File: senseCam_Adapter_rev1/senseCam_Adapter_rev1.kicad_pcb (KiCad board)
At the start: 2 copper layers, 66 x 46 mm, 11 parts, among them J1 Conn_01x30, J2 Conn_01x30, J3 Conn_01x08, J4 Conn_01x06, P1 CONN_02X05, Q1 Q_PMOS_DGS, SW1 SW_SPST, SW2 SW_Push

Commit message: SenseCam adapter board done
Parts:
- added C10: 0.1nF, sense:C_0805, F.Cu at (28.5, 38.5)
- added C12: 100nF, sense:C_0805, F.Cu at (98.0, 20.5)
- added C13: 100nF, sense:C_0805, F.Cu at (43.5, 20.5)
- added C14: 100nF, sense:C_0805, F.Cu at (30.5, 20.5)
- added C15: 100nF, sense:C_0805, F.Cu at (85.5, 20.5)
- added C3: 0.47uF, sense:C_0805, F.Cu at (89.0, 21.0)
- added C4: 0.47uF, sense:C_0805, F.Cu at (34.5, 21.0)
- added C5: 0.1nF, sense:C_0805, F.Cu at (96.0, 38.5)
- added C6: 0.1nF, sense:C_0805, F.Cu at (41.5, 38.5)
- added C7: 0.47uF, sense:C_0805, F.Cu at (76.5, 21.0)
- added C8: 0.47uF, sense:C_0805, F.Cu at (21.5, 21.0)
- added C9: 0.1nF, sense:C_0805, F.Cu at (83.5, 38.5)
- added G***: LOGO, sense:OSHW1, B.Cu at (69.4, 35.7)
- added G***: Appiko_LOGO_img, sense:Appiko_LOGO_img, F.Cu at (61.9, 28.4)
- added J5: LDR_CONN, sense:Pin_Header_Straight_1x02_Pitch2.54mm, F.Cu at (21.0, 52.0)
- added J6: Conn_01x03, sense:TerminalBlock_bornier-3_P5.08mm, F.Cu at (84.0, 14.5)
- added J7: Conn_01x03, sense:TerminalBlock_bornier-3_P5.08mm, F.Cu at (28.0, 14.5)
- added J8: Conn_01x02, sense:PinHeader_1x02_P2.54mm_Vertical, F.Cu at (63.3, 51.9)
- added R1: 10k, sense:R_0805, F.Cu at (20.0, 49.5)
- added R2: 0R033, sense:R_2512_6332Metric_Pad1.52x3.35mm_HandSolder, F.Cu at (91.0, 38.5)
- added R3: 0R033, sense:R_2512_6332Metric_Pad1.52x3.35mm_HandSolder, F.Cu at (36.5, 38.5)
- added R4: 0R033, sense:R_2512_6332Metric_Pad1.52x3.35mm_HandSolder, F.Cu at (78.5, 38.5)
- added R5: 0R033, sense:R_2512_6332Metric_Pad1.52x3.35mm_HandSolder, F.Cu at (23.5, 38.5)
- added U1: STCS2A, sense:STCS2A_PowerSO-10, F.Cu at (94.0, 28.0)
- added U2: STCS2A, sense:STCS2A_PowerSO-10, F.Cu at (39.5, 28.0)
- added U3: STCS2A, sense:STCS2A_PowerSO-10, F.Cu at (81.5, 28.0)
- added U4: STCS2A, sense:STCS2A_PowerSO-10, F.Cu at (26.5, 28.0)
- BT1: value Battery -> LiPo 2s; footprint sense:Molex_KK-6410-02_02x2.54mm_Straight -> sense:TerminalBlock_bornier-2_P5.08mm
- C1: value 10uF -> 100uF; footprint sense:C_0805_HandSoldering -> sense:CP_Elec_8x10.5
- C2: value C -> 100nF; footprint sense:C_0603_HandSoldering -> sense:C_0805
- J2: footprint Connector_FFC-FPC:Hirose_FH12-30S-0.5SH_1x30-1MP_P0.50mm_Horizontal -> sense:Hirose_FH12-30S-0.5SH_1x30-1MP_P0.50mm_Horizontal
- J3: footprint Connector_PinHeader_2.54mm:PinHeader_1x08_P2.54mm_Vertical -> sense:PinHeader_1x08_P2.54mm_Vertical; moved to F.Cu
- J4: footprint Connector_PinHeader_2.54mm:PinHeader_1x06_P2.54mm_Vertical -> sense:PinHeader_1x06_P2.54mm_Vertical; moved to F.Cu
- Q1: value Q_PMOS_DGS -> IRF9540; footprint sense:SOT-23 -> sense:TO-220-3_Vertical
- moved SW1 58.5 mm to (87.7, 52.1), turned to 180 degrees
- moved Q1 58.5 mm to (89.1, 45.3), turned to 180 degrees
- moved BT1 57.5 mm to (96.0, 50.5), turned to 90 degrees
- moved C1 52.2 mm to (76.7, 49.5)
- moved C2 33.8 mm to (47.5, 47.0), turned to 180 degrees
- moved SW2 32.8 mm to (48.5, 51.5), turned to 180 degrees
- moved J3 17.8 mm to (15.0, 16.4)
- moved J4 12.7 mm to (15.0, 39.2)
- moved J2 9.00 mm to (61.5, 42.0)
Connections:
- net Net-(J3-Pad5) renamed /5V
- net Net-(P1-Pad2) renamed /SENSE_JACK
- C1 pad 1: VDD -> /VIN
- J1 pad 2: /FLASH -> /CAM_FLASH
- J1 pad 3: /TRIGGER -> /CAM_TRIGGER
- J3 pad 4: Net-(J3-Pad4) -> /3V3
- J3 pad 6: Net-(J3-Pad6) -> GND
- J3 pad 7: Net-(J3-Pad7) -> GND
- J3 pad 8: Net-(J3-Pad8) -> /VIN
- J4 pad 1: /TRIGGER -> /FLASH_TRIGGER
- J4 pad 2: Net-(J4-Pad2) -> /CAM_FLASH
- J4 pad 3: Net-(J4-Pad3) -> /CAM_TRIGGER
- J4 pad 4: Net-(J4-Pad4) -> /FOCUS
- J4 pad 5: Net-(J4-Pad5) -> /SENSE_TRIGGER
- J4 pad 6: Net-(J4-Pad6) -> /LDR
- P1 pad 3: Net-(P1-Pad3) -> /STM_TX
- P1 pad 4: Net-(P1-Pad4) -> /FOCUS
- P1 pad 5: Net-(P1-Pad5) -> /STM_RX
- P1 pad 6: /TRIGGER -> /SENSE_TRIGGER
- P1 pad 8: VDD -> /3V3
- Q1 pad 2: VDD -> Net-(Q1-Pad2)
- Q1 pad 3: Net-(Q1-Pad3) -> /VIN
- SW1 pad 2: Net-(Q1-Pad3) -> Net-(Q1-Pad2)
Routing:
- net /VIN: track 0.00 -> 205.5 mm
- net /3V3: track 0.00 -> 131.0 mm
- net GND: track 0.00 -> 129.8 mm, vias 0 -> 8
- net /FLASH_TRIGGER: track 0.00 -> 116.3 mm, vias 0 -> 4
- net /CAM_TRIGGER: track 0.00 -> 63.1 mm
- net /CAM_FLASH: track 0.00 -> 60.9 mm
- net /DCMI_VSYNC: track 0.00 -> 33.0 mm, vias 0 -> 2
- net /D9: track 0.00 -> 32.5 mm, vias 0 -> 2
- net /STM_RX: track 0.00 -> 31.8 mm
- net /D8: track 0.00 -> 31.7 mm, vias 0 -> 2
- net /DCMI_HSYNC: track 0.00 -> 31.7 mm, vias 0 -> 2
- net /D7: track 0.00 -> 31.5 mm, vias 0 -> 2
- net /D6: track 0.00 -> 31.2 mm, vias 0 -> 2
- net /D10: track 0.00 -> 31.2 mm, vias 0 -> 2
- net /D5: track 0.00 -> 30.8 mm, vias 0 -> 2
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- added copper zone on B.Cu, net GND
- added copper zone on F.Cu, net GND
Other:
- board size 66 x 46 mm -> 90 x 46 mm
- net class Power added: clearance 0.2, trace_width 1, via_dia 0.8, via_drill 0.4
- net class Power+ added: clearance 0.2, trace_width 1.5, via_dia 0.8, via_drill 0.4
- board text added: "Appiko"
- board text added: "SenseCam Disco Adapter v1"

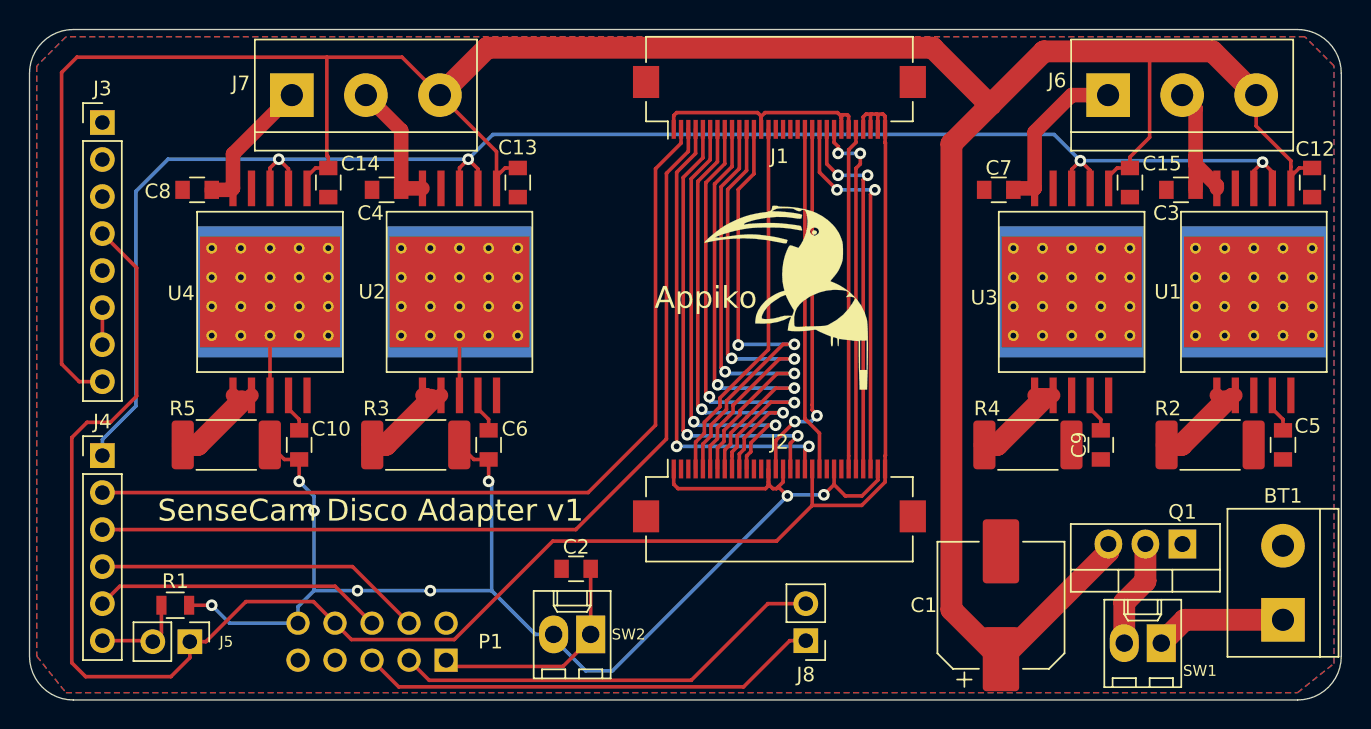
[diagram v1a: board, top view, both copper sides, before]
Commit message: Update the PCB with change in
- battery connector, buffer cap and reverse polarity protection MOSFET
- SenseBe connector orientation
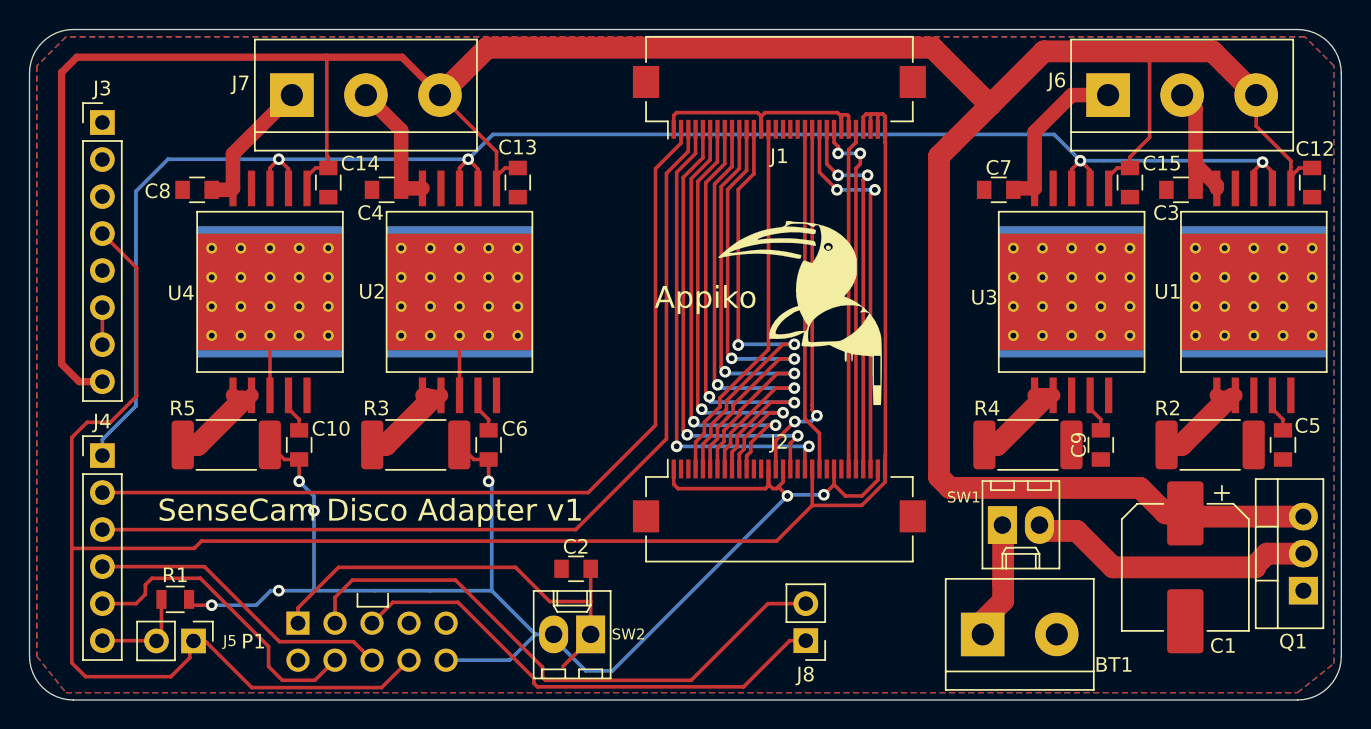
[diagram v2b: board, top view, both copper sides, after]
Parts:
- added ?: KiCad-Logo2_8mm_SilkScreen, sense:KiCad-Logo2_8mm_SilkScreen, B.Cu at (87.0, 36.6)
- moved G*** 28.4 mm to (41.5, 40.5)
- moved BT1 20.6 mm to (75.4, 51.5), turned to 0 degrees
- moved SW1 13.6 mm to (76.8, 44.0), turned to 0 degrees
- moved C1 12.9 mm to (89.3, 46.9), turned to 270 degrees
- moved Q1 8.90 mm to (97.4, 48.5), turned to 90 degrees
- moved G*** 1.42 mm to (62.9, 29.4)
- moved R1 0.40 mm to (20.0, 49.1)
- moved J5 0.25 mm to (21.2, 52.0)
- turned P1 to 0 degrees
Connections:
- J4 pad 4: /FOCUS -> /SENSE_TRIGGER
- J4 pad 5: /SENSE_TRIGGER -> /FOCUS
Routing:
- net /3V3: track 131.0 -> 151.4 mm
- net /BUTTON: track 15.7 -> 30.7 mm
- net Net-(Q1-Pad2): track 7.40 -> 19.6 mm
- net /STM_TX: track 30.0 -> 40.0 mm
- net GND: track 129.8 -> 135.6 mm, vias 8 -> 7
- net /STM_RX: track 31.8 -> 34.3 mm
- net Net-(BT1-Pad1): track 9.01 -> 7.68 mm
- net /FOCUS: track 22.6 -> 21.3 mm
- net /SENSE_TRIGGER: track 20.0 -> 21.2 mm
- net /VIN: track 205.5 -> 206.3 mm

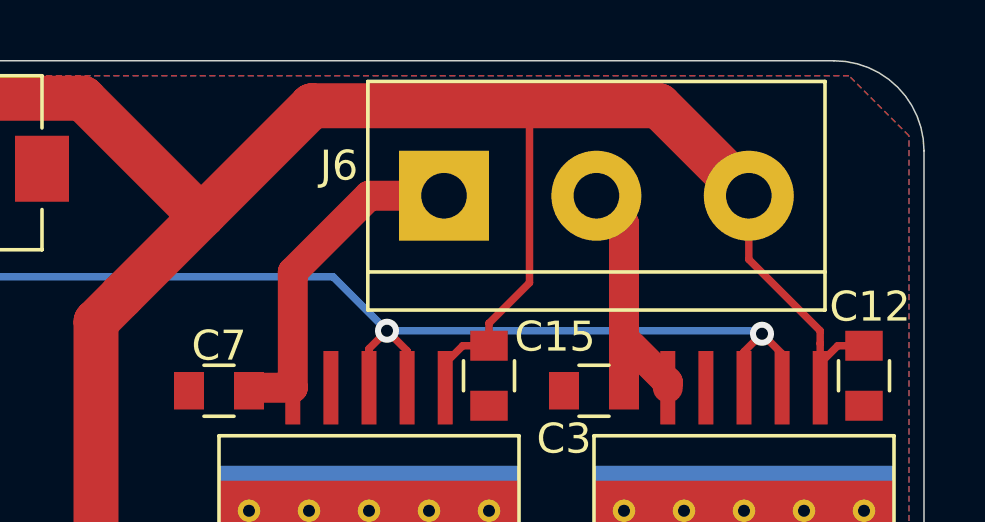
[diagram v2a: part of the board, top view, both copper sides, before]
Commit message: Move the LED connector a bit to the corner
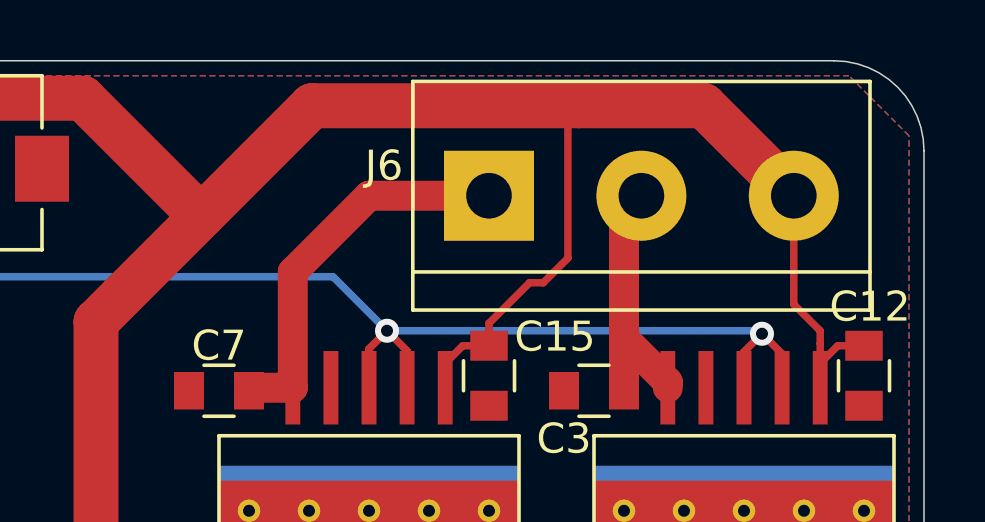
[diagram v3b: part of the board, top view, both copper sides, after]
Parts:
- moved J6 1.50 mm to (85.5, 14.5)
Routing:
- net /VIN: track 206.3 -> 208.8 mm
- net /LED1: track 9.64 -> 8.33 mm
